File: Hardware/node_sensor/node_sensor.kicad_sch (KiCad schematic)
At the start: 12 parts, among them J1 Solar_Pannel, U1 TPS63020, U2 INA219, U3 E32-433, U4 DevKitSTM32, U5 BMP-388, U6 SHT30

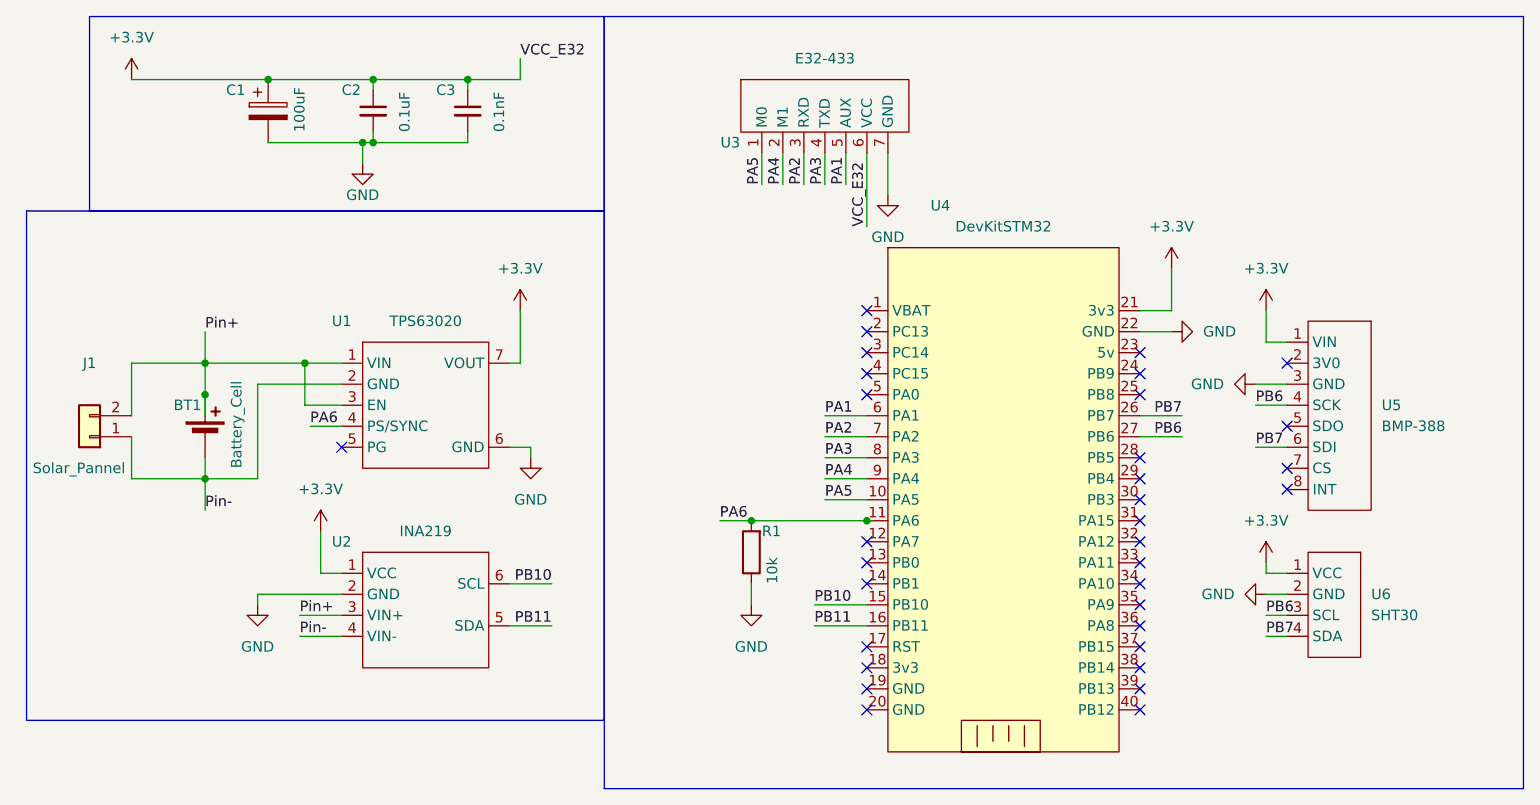
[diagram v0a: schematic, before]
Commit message: completed node_sensor v1.1
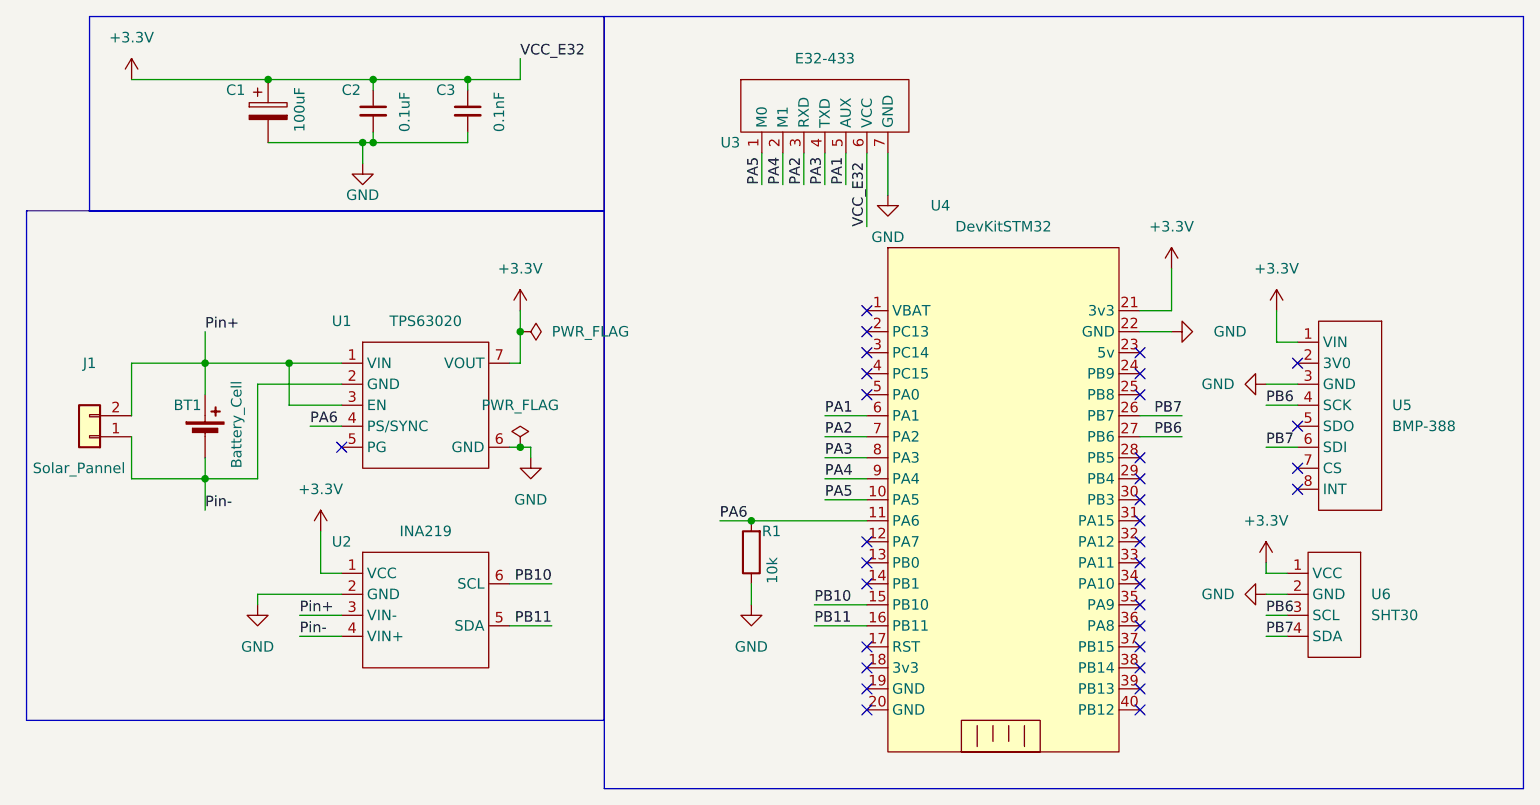
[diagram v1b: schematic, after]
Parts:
- J1: footprint (none) -> iot_footprint:XH 2.54 2Pin Female
- R1: footprint (none) -> iot_footprint:R0603
- U1: footprint (none) -> course_kicad_ecp_footprint:TPS63020-module; symbol Course_elpcb:TPS63020 -> Course_elpcb:TPS63020-Rakstore-board
- U5: footprint Connector_PinSocket_2.54mm:PinSocket_1x08_P2.54mm_Vertical -> course_kicad_ecp_footprint:BMP388-module
